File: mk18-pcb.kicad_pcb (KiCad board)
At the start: 2 copper layers, 153.9 x 71.7 mm, 49 parts, among them J1 RESET, J10 MACRO-1, J11 MACRO-2, J12 BYPASS MACRO, J13 Fal1-Col-Select, J14 Fal2-Col-Select, J15 Fal1-Row-Select, J16 Fal2-Row-Select, J17 RKJXT-MTX, J18 RKJXT-EC11, J19 Fal2-Col-Select, J2 BYPASS FAL1, J21 Fal2-Col-Select, J3 BYPASS FAL2, J4 BYPASS IND, J5 BYPASS PEDALS, J6 BYPASS SCREEN, J7 Falcon1, J8 Falcon2, J9 PMW JST, U1 TYPE-C-31-M-12, U10 1N4148W_C81598, U11 1N4148W_C81598, U12 1N4148W_C81598, U13 1N4148W_C81598, U14 1N4148W_C81598, U15 1N4148W_C81598, U2 ECT818001569, U3 TYPE-C-31-M-12, U4 Pico, U5 TYPE-C-31-M-12, U6 AO3401A_C347476, U7 SRV0504, U8 74LVC1T45, U9 1N4148W_C81598

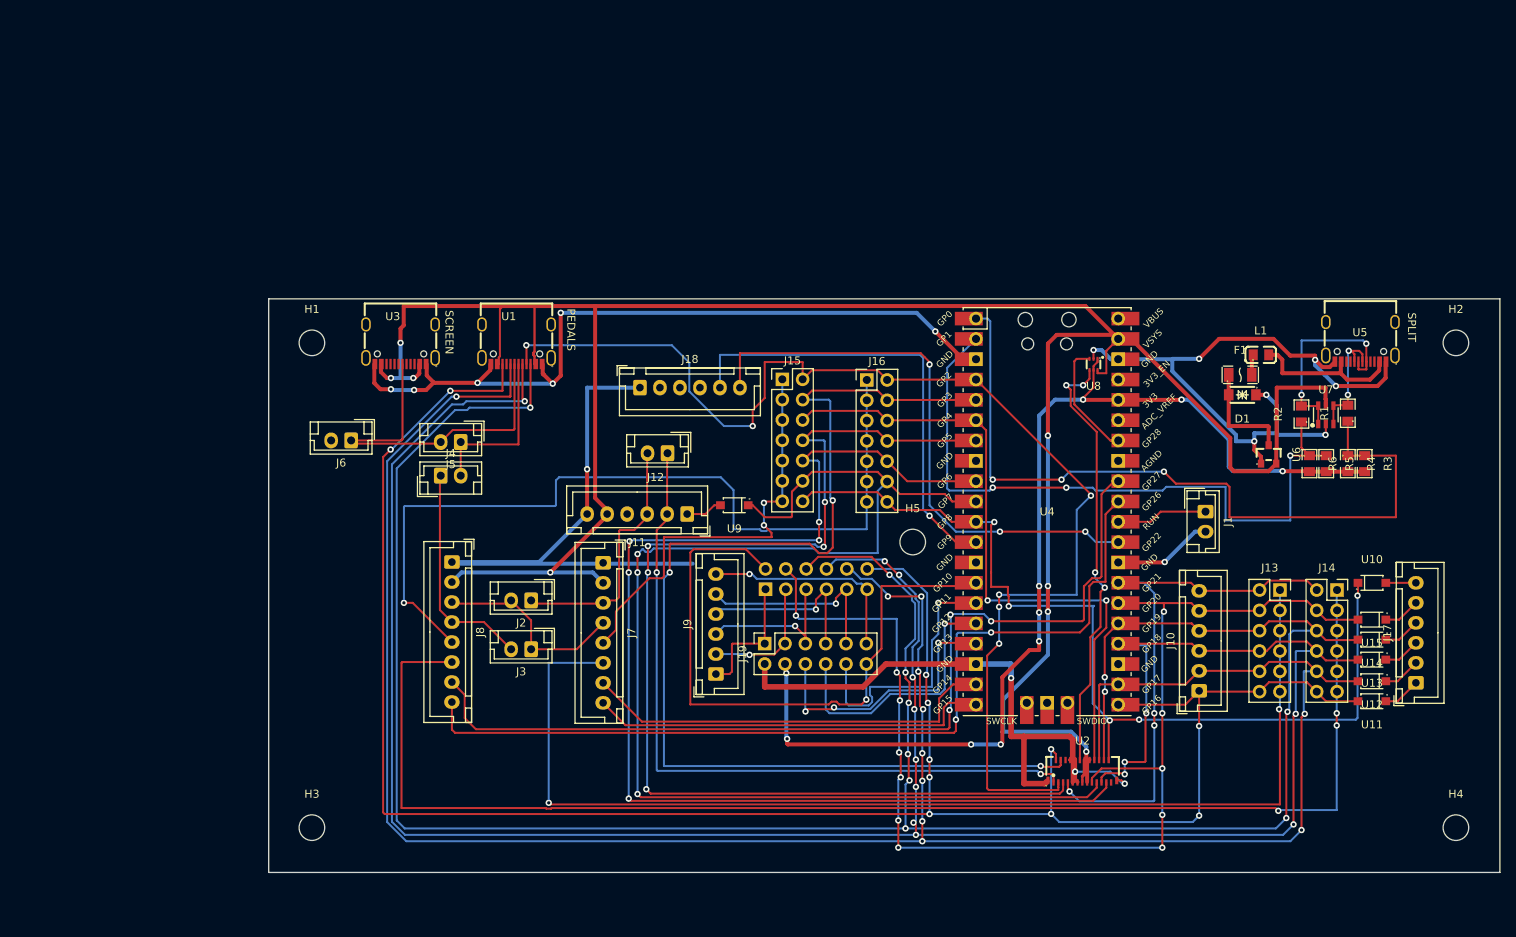
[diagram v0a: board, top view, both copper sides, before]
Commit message: jan2 updates, relocating shift registers
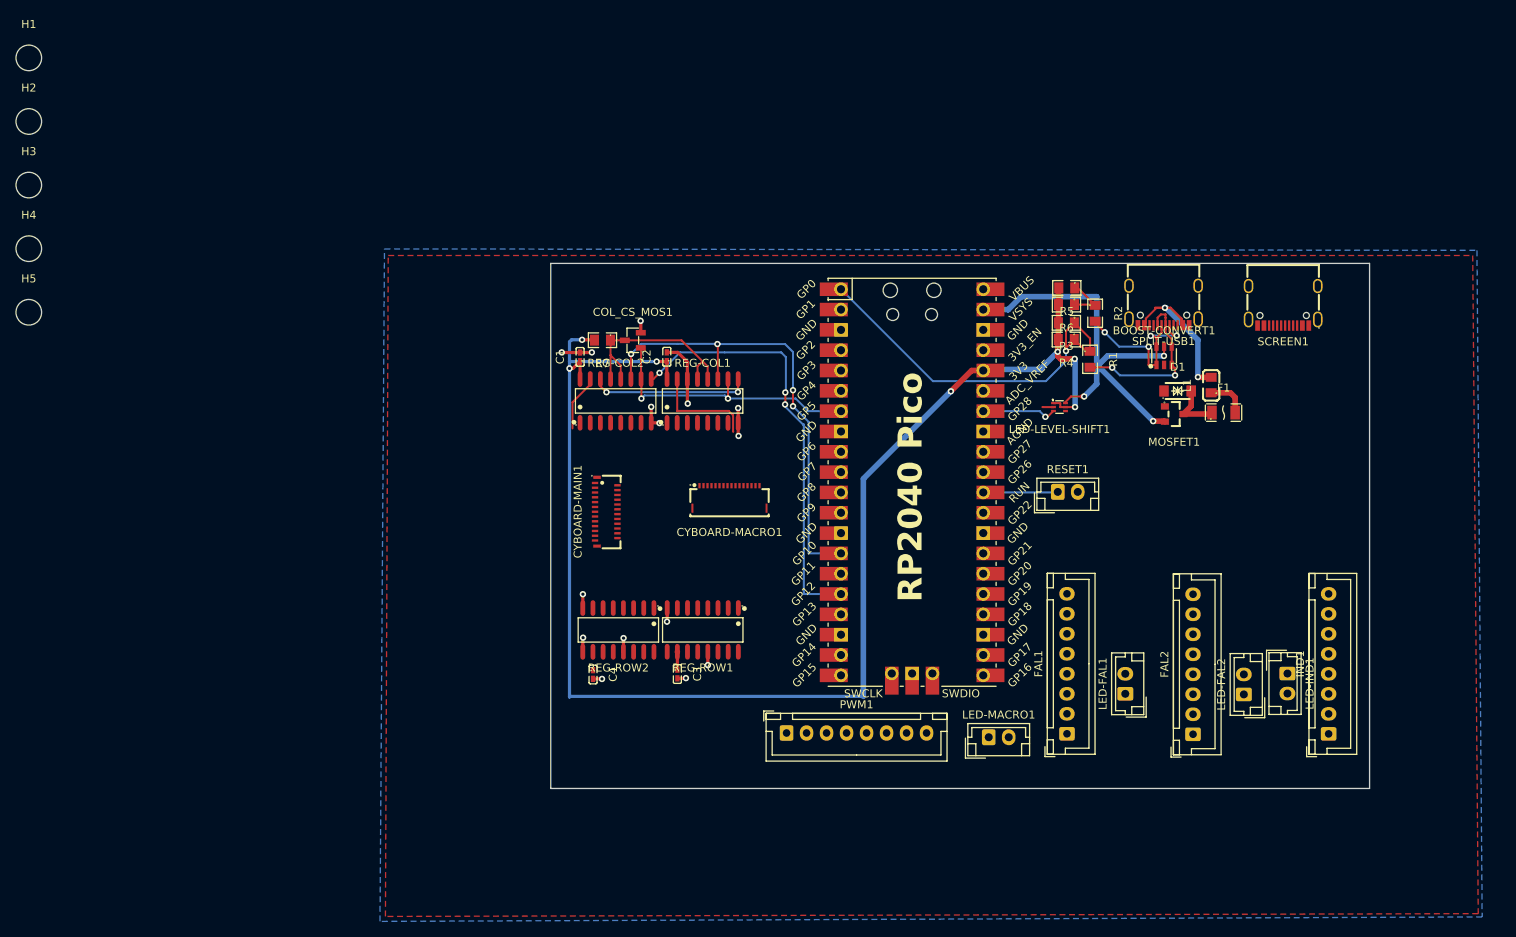
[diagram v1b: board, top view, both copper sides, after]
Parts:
- removed J1: RESET, Connector_JST:JST_EH_B2B-EH-A_1x02_P2.50mm_Vertical
- removed J10: MACRO-1, Connector_JST:JST_XH_B6B-XH-A_1x06_P2.50mm_Vertical
- removed J11: MACRO-2, Connector_JST:JST_XH_B6B-XH-A_1x06_P2.50mm_Vertical
- removed J12: BYPASS MACRO, Connector_JST:JST_EH_B2B-EH-A_1x02_P2.50mm_Vertical
- removed J13: Fal1-Col-Select, Connector_PinSocket_2.54mm:PinSocket_2x06_P2.54mm_Vertical
- removed J14, J19, J21: Fal2-Col-Select, Connector_PinSocket_2.54mm:PinSocket_2x06_P2.54mm_Vertical
- removed J15: Fal1-Row-Select, Connector_PinHeader_2.54mm:PinHeader_2x07_P2.54mm_Vertical
- removed J16: Fal2-Row-Select, Connector_PinHeader_2.54mm:PinHeader_2x07_P2.54mm_Vertical
- removed J17: RKJXT-MTX, Connector_JST:JST_XH_B6B-XH-A_1x06_P2.50mm_Vertical
- removed J18: RKJXT-EC11, Connector_JST:JST_XH_B6B-XH-A_1x06_P2.50mm_Vertical
- removed J2: BYPASS FAL1, Connector_JST:JST_EH_B2B-EH-A_1x02_P2.50mm_Vertical
- removed J3: BYPASS FAL2, Connector_JST:JST_EH_B2B-EH-A_1x02_P2.50mm_Vertical
- removed J4: BYPASS IND, Connector_JST:JST_EH_B2B-EH-A_1x02_P2.50mm_Vertical
- removed J5: BYPASS PEDALS, Connector_JST:JST_EH_B2B-EH-A_1x02_P2.50mm_Vertical
- removed J6: BYPASS SCREEN, Connector_JST:JST_EH_B2B-EH-A_1x02_P2.50mm_Vertical
- removed J7: Falcon1, Connector_JST:JST_XH_B8B-XH-A_1x08_P2.50mm_Vertical
- removed J8: Falcon2, Connector_JST:JST_XH_B8B-XH-A_1x08_P2.50mm_Vertical
- removed J9: PMW JST, Connector_JST:JST_XH_B6B-XH-A_1x06_P2.50mm_Vertical
- removed U1, U3, U5: TYPE-C-31-M-12, kicad-library:USB-C_SMD-TYPE-C-31-M-12
- removed U10, U11, U12, U13, U14, U15, U9: 1N4148W_C81598, kicad-library:SOD-123F_L2.7-W1.6-LS3.8-RD
- removed U2: ECT818001569, kicad-library:FPC-SMD_ECT818001569
- removed U4: Pico, rp2040:RPi_Pico_SMD_TH
- removed U6: AO3401A_C347476, kicad-library:SOT-23_L2.9-W1.3-P1.90-LS2.4-BR
- removed U7: SRV0504, kicad-library:SOT-23-6_L2.9-W1.6-P0.95-LS2.8-BL
- removed U8: 74LVC1T45, kicad-library:SOT-5X3-6_W1.6-L1.2-P0.50-LS1.6-BL
- added BOOST-CONVERT1: SRV0504, ct-kicad:SOT-23-6_L2.9-W1.6-P0.95-LS2.8-BL, F.Cu at (191.5, 82.6)
- added C1: 100nF, ct-kicad:C0402, F.Cu at (118.5, 82.8)
- added C2: 100nF, ct-kicad:C0402, F.Cu at (129.4, 82.7)
- added C3: 100nF, ct-kicad:C0402, F.Cu at (130.7, 122.4)
- added C4: 100nF, ct-kicad:C0402, F.Cu at (120.1, 122.5)
- added COL_CS_MOS1: 2N7002, ct-kicad:SOT-23-3_L2.9-W1.3-P1.90-LS2.4-BR, F.Cu at (125.1, 80.7)
- added CYBOARD-MACRO1: HC-FPC-05-10-16RLTAG, ct-kicad:FPC-SMD_16P-P0.50_HCTL_HC-FPC-05-10-16RLTAG, F.Cu at (137.2, 100.3)
- added CYBOARD-MAIN1: ECT818001569, ct-kicad:FPC-SMD_ECT818001569, F.Cu at (121.8, 102.1)
- added FAL1: Conn_01x08_Socket, Connector_JST:JST_XH_B8B-XH-A_1x08_P2.50mm_Vertical, F.Cu at (179.4, 129.9)
- added FAL2: Conn_01x08_Socket, Connector_JST:JST_XH_B8B-XH-A_1x08_P2.50mm_Vertical, F.Cu at (195.1, 129.9)
- added IND1: Conn_01x08_Socket, Connector_JST:JST_XH_B8B-XH-A_1x08_P2.50mm_Vertical, F.Cu at (212.1, 129.9)
- added LED-FAL1: Conn_01x02_Socket, Connector_JST:JST_EH_B2B-EH-A_1x02_P2.50mm_Vertical, F.Cu at (186.7, 124.9)
- added LED-FAL2: Conn_01x02_Socket, Connector_JST:JST_EH_B2B-EH-A_1x02_P2.50mm_Vertical, F.Cu at (201.5, 125.0)
- added LED-IND1: Conn_01x02_Socket, Connector_JST:JST_EH_B2B-EH-A_1x02_P2.50mm_Vertical, F.Cu at (206.9, 122.3)
- added LED-LEVEL-SHIFT1: SN74LVC1T45DRL, ct-kicad:SOT-563_L1.6-W1.2-P0.50-LS1.6-BR, F.Cu at (178.4, 89.0)
- added LED-MACRO1: Conn_01x02_Socket, Connector_JST:JST_EH_B2B-EH-A_1x02_P2.50mm_Vertical, F.Cu at (169.6, 130.3)
- added MOSFET1: AO3401A_C347476, ct-kicad:SOT-23_L2.9-W1.3-P1.90-LS2.4-BR, F.Cu at (192.8, 89.9)
- added PICO1: Pico, rp2040:RPi_Pico_SMD_TH, F.Cu at (160.0, 98.4)
- added PWM1: Conn_01x08_Socket, Connector_JST:JST_XH_B8B-XH-A_1x08_P2.50mm_Vertical, F.Cu at (144.3, 129.8)
- added R7: RK73H2ATTD9101F, ct-kicad:R0805, F.Cu at (121.3, 80.7)
- added REG-COL1: MC74HC589ADR2G, ct-kicad:SOIC-16_L9.9-W3.9-P1.27-LS6.0-BL, F.Cu at (133.8, 88.3)
- added REG-COL2: MC74HC589ADR2G, ct-kicad:SOIC-16_L9.9-W3.9-P1.27-LS6.0-BL, F.Cu at (123.0, 88.3)
- added REG-ROW1: 74HC595D, ct-kicad:SOIC-16_L9.9-W3.9-P1.27-LS6.0-BL, F.Cu at (133.9, 116.9)
- added REG-ROW2: 74HC595D, ct-kicad:SOIC-16_L9.9-W3.9-P1.27-LS6.0-BL, F.Cu at (123.3, 116.9)
- added RESET1: Conn_01x02_Socket, Connector_JST:JST_EH_B2B-EH-A_1x02_P2.50mm_Vertical, F.Cu at (178.2, 99.6)
- added SCREEN1: TYPE-C-31-M-12, ct-kicad:USB-C_SMD-TYPE-C-31-M-12, F.Cu at (206.4, 76.4)
- added SPLIT-USB1: TYPE-C-31-M-12, ct-kicad:USB-C_SMD-TYPE-C-31-M-12, F.Cu at (191.5, 76.3)
- D1: footprint kicad-library:SOD-123FL_L2.8-W1.8-LS3.7-BI -> ct-kicad:SOD-123FL_L2.8-W1.8-LS3.7-BI
- F1: footprint kicad-library:F1206 -> ct-kicad:F1206
- L1: footprint kicad-library:L0805 -> ct-kicad:L0805
- R1, R2, R3, R4, R5, R6: footprint kicad-library:R0805 -> ct-kicad:R0805
- moved H4 192.5 mm to (49.6, 69.2)
- moved H2 180.5 mm to (49.6, 53.3)
- moved H5 114.2 mm to (49.6, 77.2)
- moved H3 87.8 mm to (49.6, 61.3)
- moved H1 50.2 mm to (49.6, 45.4)
- moved R3 41.2 mm to (179.3, 78.5), turned to 180 degrees
- moved R5 39.2 mm to (179.4, 74.1), turned to 180 degrees
- moved R4 38.5 mm to (179.3, 80.6), turned to 180 degrees
- moved R6 36.3 mm to (179.3, 76.2), turned to 180 degrees
- moved R1 32.9 mm to (182.3, 83.1), turned to -90 degrees
- moved R2 28.7 mm to (182.9, 77.3), turned to -90 degrees
- moved D1 8.10 mm to (193.2, 87.0), turned to 0 degrees
- moved L1 7.28 mm to (197.4, 86.3), turned to 90 degrees
- moved F1 5.16 mm to (199.0, 89.7)
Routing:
- net GND: track 345.8 -> 32.3 mm, vias 18 -> 15
- net col3: track 310.2 -> 0.00 mm, vias 14 -> 0
- net col4: track 304.0 -> 0.00 mm, vias 11 -> 0
- net col2: track 291.4 -> 0.00 mm, vias 11 -> 0
- net col1: track 263.0 -> 0.00 mm, vias 11 -> 0
- net VCC: track 312.6 -> 52.2 mm, vias 8 -> 3
- net fal2-col: track 169.1 -> 0.00 mm, vias 3 -> 0
- net row6: track 163.8 -> 0.00 mm, vias 3 -> 0
- net col5: track 153.6 -> 0.00 mm, vias 12 -> 0
- net row1: track 153.2 -> 0.00 mm, vias 6 -> 0
- net row5: track 152.8 -> 0.00 mm, vias 5 -> 0
- net row4: track 144.9 -> 0.00 mm, vias 5 -> 0
- net row2: track 144.3 -> 0.00 mm, vias 3 -> 0
- net fal1-col: track 142.7 -> 0.00 mm, vias 2 -> 0
- net row7: track 118.0 -> 0.00 mm, vias 5 -> 0
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- added copper zone on B.Cu, net GND
- added copper zone on F.Cu, net GND
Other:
- board size 153.9 x 71.7 mm -> 102.4 x 65.6 mm
- board text added: "RP2040 Pico"
- board text removed: "PEDALS"
- board text removed: "SCREEN"
- board text removed: "SPLIT"

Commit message: adding design rules and jan3 updates.  needs review now.
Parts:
- moved LED-MACRO1 46.5 mm to (139.6, 94.8)
- moved PWM1 11.2 mm to (155.5, 129.6), turned to 180 degrees
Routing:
- net VCC: track 52.2 -> 286.6 mm, vias 3 -> 15
- net LED_FAL1_DI: track 0.00 -> 161.1 mm, vias 0 -> 7
- net GND: track 32.3 -> 162.3 mm, vias 15 -> 45
- net LED_KEYS_DI: track 0.00 -> 116.5 mm, vias 0 -> 2
- net SPI1_CLK: track 58.7 -> 116.7 mm, vias 4 -> 9
- net LED_INDICATORS_DO: track 0.00 -> 54.0 mm, vias 0 -> 3
- net SPI1_MOSI: track 0.00 -> 50.0 mm, vias 0 -> 3
- net ROW_CS: track 0.00 -> 46.2 mm, vias 0 -> 6
- net +3V3: track 183.2 -> 224.6 mm, vias 7 -> 12
- net col7: track 0.00 -> 36.6 mm, vias 0 -> 4
- net Split_Comms_RX: track 6.05 -> 41.3 mm, vias 0 -> 2
- net row3: track 0.00 -> 32.8 mm, vias 0 -> 6
- net row0: track 0.00 -> 30.8 mm, vias 0 -> 4
- net col3: track 0.00 -> 28.7 mm, vias 0 -> 4
- net fal2-r2: track 0.00 -> 28.3 mm
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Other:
- board size 102.4 x 65.6 mm -> 108.8 x 65.6 mm
- board text added: "-->"
- board text added: "Cyboard Main"
- board text added: "FAL1"
- board text added: "FAL2"
- board text added: "IND1"
- board text added: "Macropad"
- board text added: "TO SCREEN IND's"
- board text added: "TO SPLIT"

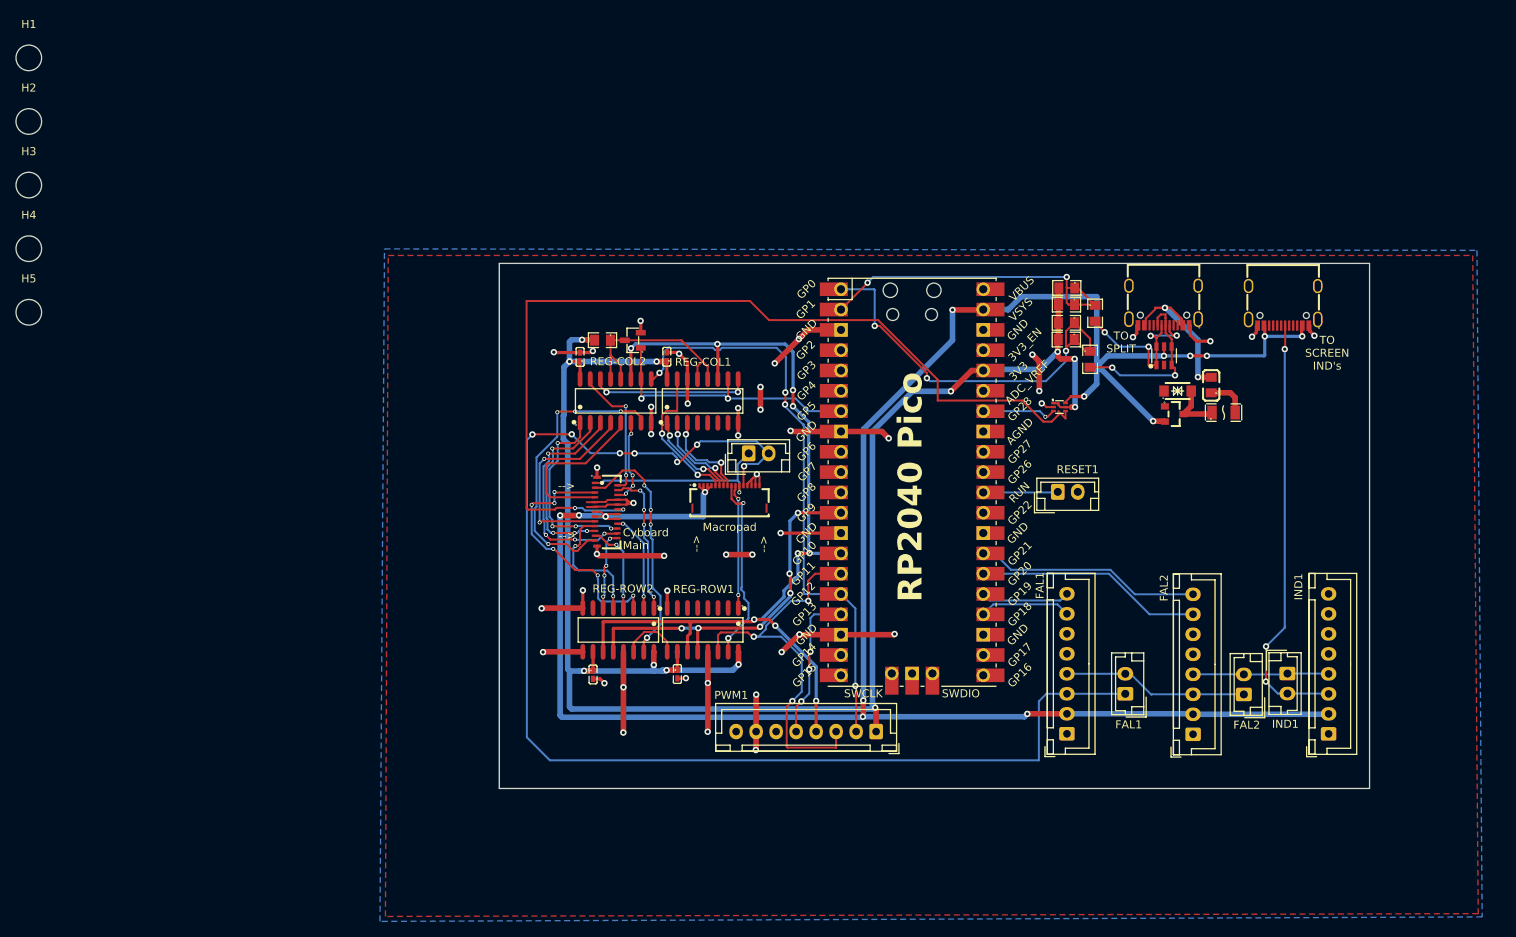
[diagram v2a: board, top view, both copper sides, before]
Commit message: getting ready to re-do the shift register routing so we can have pinouts.
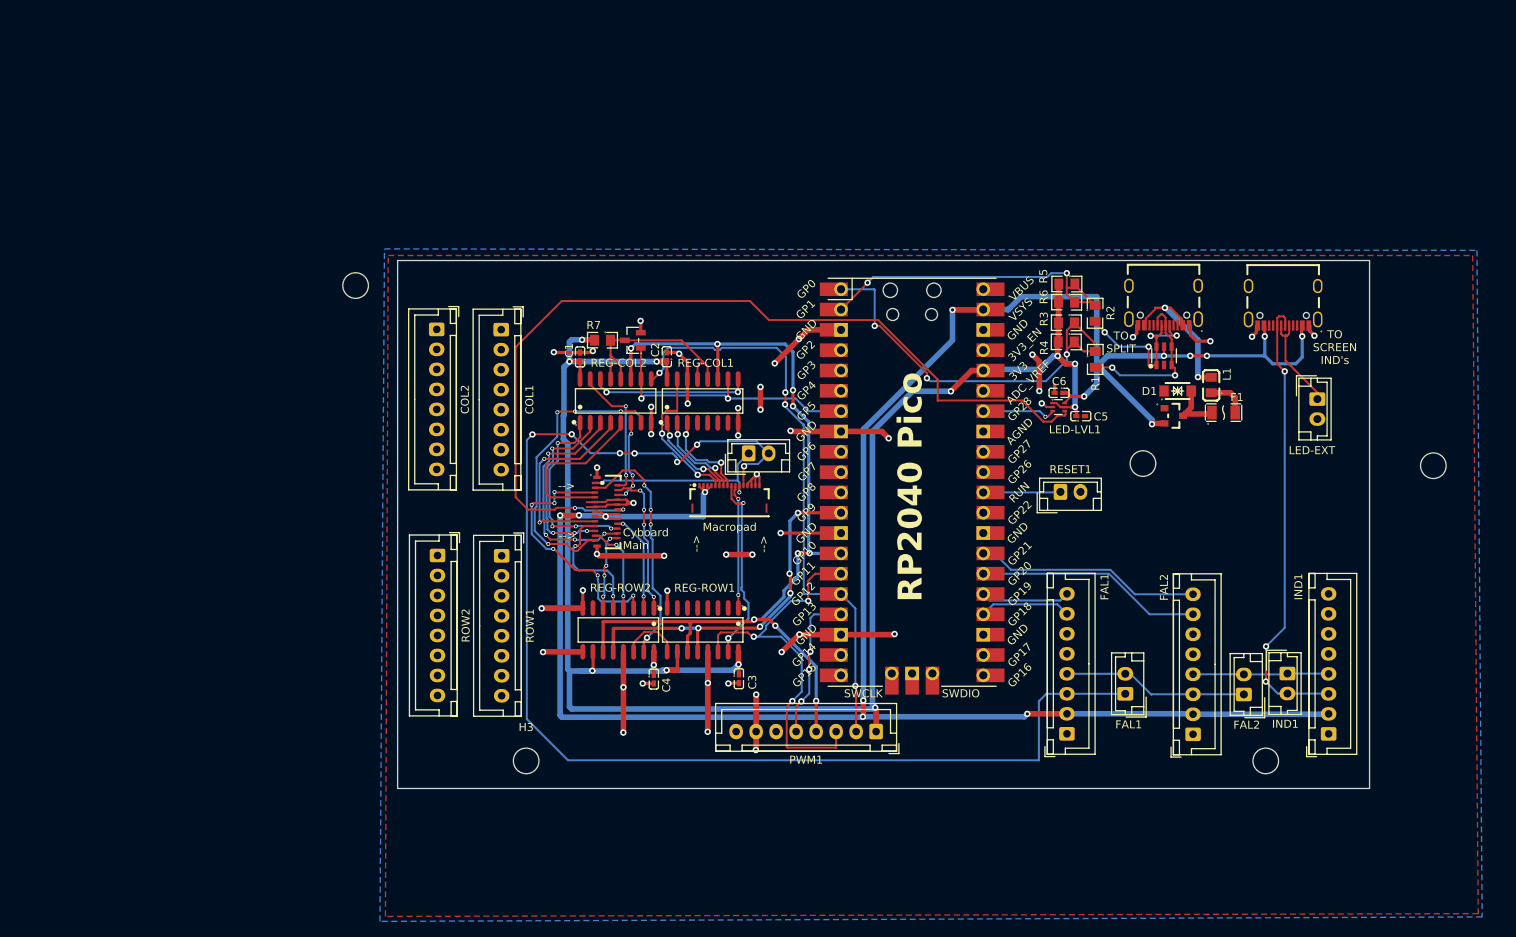
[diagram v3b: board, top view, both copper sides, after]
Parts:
- removed LED-LEVEL-SHIFT1: SN74LVC1T45DRL, ct-kicad:SOT-563_L1.6-W1.2-P0.50-LS1.6-BR
- added C5: 100nF, ct-kicad:C0402, F.Cu at (181.1, 90.2)
- added C6: 100nF, ct-kicad:C0402, F.Cu at (178.4, 87.2)
- added COL1: Conn_01x08_Socket, Connector_JST:JST_XH_B8B-XH-A_1x08_P2.50mm_Vertical, F.Cu at (108.7, 79.3)
- added COL2: Conn_01x08_Socket, Connector_JST:JST_XH_B8B-XH-A_1x08_P2.50mm_Vertical, F.Cu at (100.6, 79.3)
- added LED-EXT-DO1: Conn_01x02_Socket, Connector_JST:JST_EH_B2B-EH-A_1x02_P2.50mm_Vertical, F.Cu at (210.7, 88.0)
- added LED-LVL1: SN74LVC1T45DRL, ct-kicad:SOT-563_L1.6-W1.2-P0.50-LS1.6-BR, F.Cu at (178.3, 89.0)
- added ROW1: Conn_01x08_Socket, Connector_JST:JST_XH_B8B-XH-A_1x08_P2.50mm_Vertical, F.Cu at (108.7, 107.6)
- added ROW2: Conn_01x08_Socket, Connector_JST:JST_XH_B8B-XH-A_1x08_P2.50mm_Vertical, F.Cu at (100.7, 107.6)
- moved H2 180.8 mm to (225.2, 96.4)
- moved H4 167.4 mm to (204.2, 133.3)
- moved H5 140.5 mm to (188.9, 96.1)
- moved H3 95.1 mm to (111.8, 133.3)
- moved H1 49.8 mm to (90.5, 73.8)
- moved C3 7.71 mm to (138.4, 123.0)
- moved C4 7.62 mm to (127.7, 123.0)
- moved R1 0.65 mm to (182.9, 83.1)
- moved R5 0.49 mm to (179.4, 73.7)
- moved RESET1 0.34 mm to (178.6, 99.6)
- moved R4 0.30 mm to (179.3, 80.9)
- moved R6 0.30 mm to (179.3, 75.9)
- moved MOSFET1 0.22 mm to (192.7, 90.1)
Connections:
- SCREEN1 pad A7: unconnected-(SCREEN1-DN1-PadA7) -> LED_SCREEN_DO
- SCREEN1 pad B6: unconnected-(SCREEN1-DP2-PadB6) -> LED_INDICATORS_DO
- SCREEN1 pad B7: unconnected-(SCREEN1-DN2-PadB7) -> LED_SCREEN_DO
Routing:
- net LED_SCREEN_DO: track 0.00 -> 12.8 mm
- net VCC: track 286.6 -> 291.9 mm
- net LED_INDICATORS_DO: track 54.0 -> 57.5 mm
- net +3V3: track 224.6 -> 228.0 mm
- net LED_KEYS_DI: track 116.5 -> 113.8 mm
- net LED_FAL1_DI: track 161.1 -> 159.7 mm
- net Split_Comms_TX: track 51.0 -> 52.1 mm
- net GND: track 162.3 -> 163.2 mm
- net Split_Comms_TX-A6: track 21.3 -> 20.4 mm
- net Split_Comms_RX: track 41.3 -> 41.8 mm
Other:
- board size 108.8 x 65.6 mm -> 121.5 x 66 mm
- board text added: "LED-EXT"
